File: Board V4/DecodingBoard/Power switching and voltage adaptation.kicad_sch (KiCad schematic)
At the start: 19 parts, among them U2 TPS7A7200RGW, U4 TPS2121RUXR

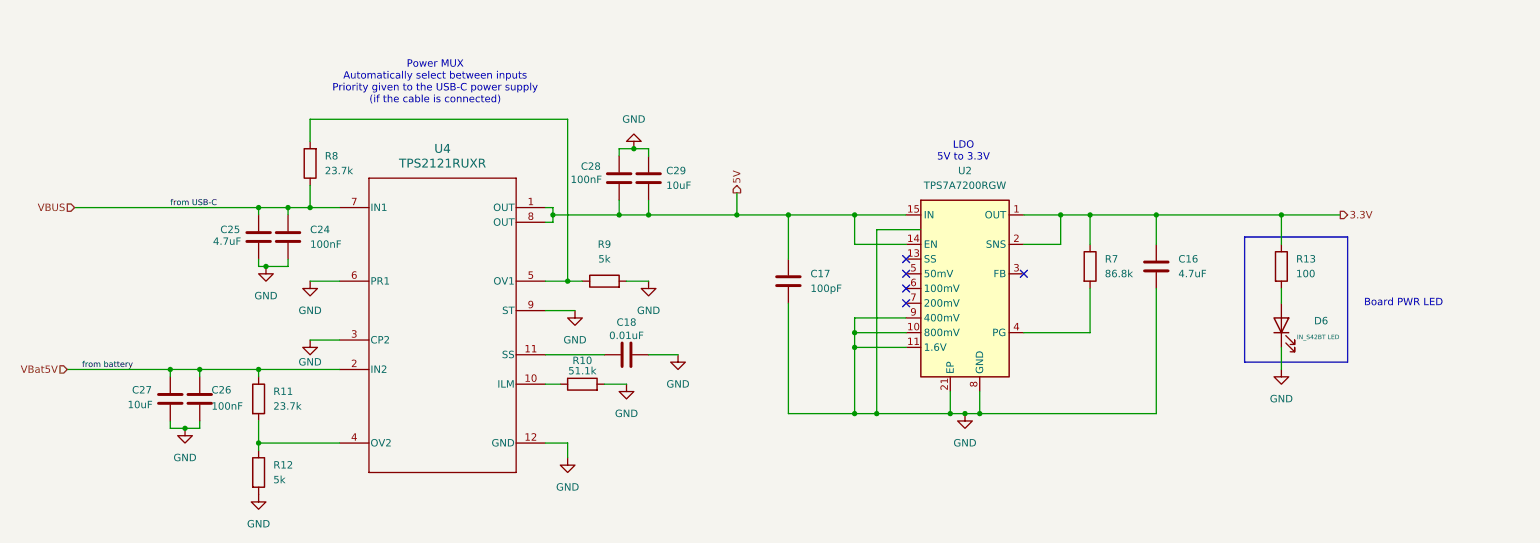
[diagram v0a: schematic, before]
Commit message: update to the LDO footprint and C16 from 4.7 uF to 10 uF
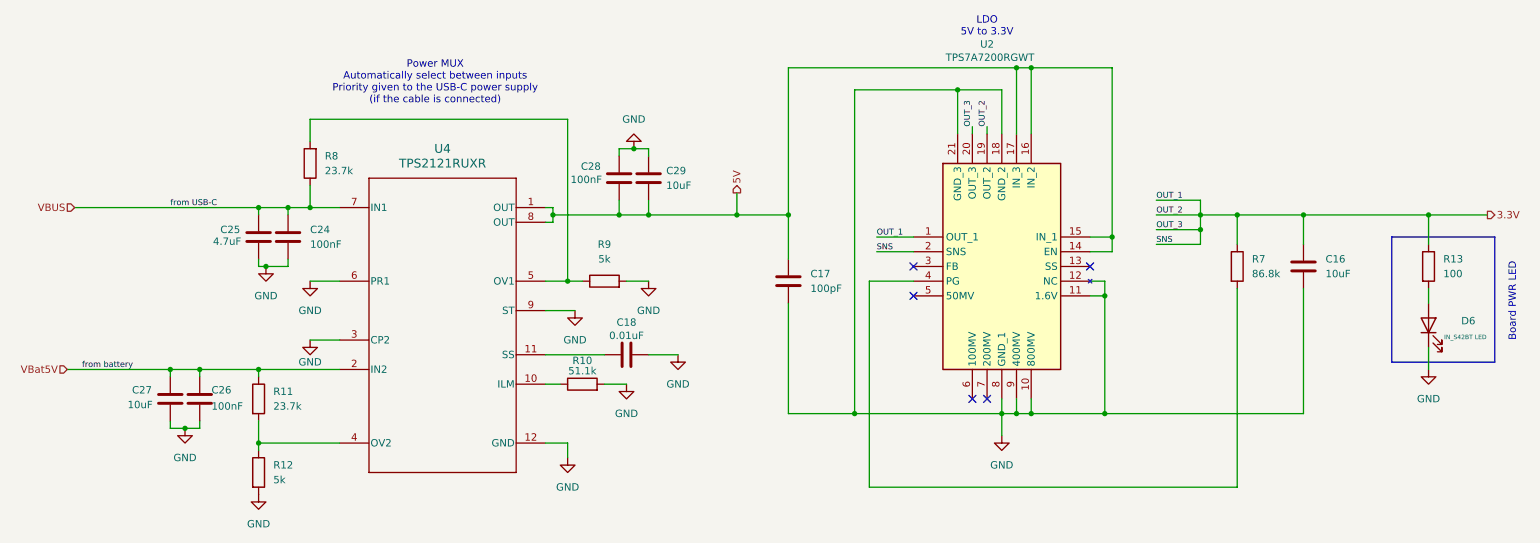
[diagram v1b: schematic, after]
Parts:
- removed U2: TPS7A7200RGW, Package_DFN_QFN:Texas_RGW0020A_VQFN-20-1EP_5x5mm_P0.65mm_EP3.15x3.15mm_ThermalVias, symbol Regulator_Linear:TPS7A7200RGW
- added U2: TPS7A7200RGWT, QFN65P500X500X100-21N-D, symbol TPS7A7200RGWT:TPS7A7200RGWT
- C16: value 4.7uF -> 10uF
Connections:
- net 3.3V: now also U2.1 (OUT_1), U2.19 (OUT_2), U2.2 (SNS), U2.20 (OUT_3)
- net 5V: now also U2.14 (EN), U2.15 (IN_1), U2.16 (IN_2), U2.17 (IN_3)
- net GND: now also U2.10 (800MV), U2.11 (1.6V), U2.12 (NC), U2.18 (GND_2), U2.21 (GND_3), U2.8 (GND_1), U2.9 (400MV)
- net at R7.2: now also U2.4 (PG)
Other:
- moved on the sheet: C16, D6, R13, R7

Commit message: Addition of the BLE module and BOM
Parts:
- C16, C17, C25, C27, C29: footprint (none) -> Capacitor_SMD:C_0603_1608Metric
- C18, C24, C26, C28: footprint (none) -> Capacitor_SMD:C_0402_1005Metric
- R10, R11, R12, R13, R8, R9: footprint (none) -> Resistor_SMD:R_0402_1005Metric
- R7: footprint (none) -> Resistor_SMD:R_0603_1608Metric
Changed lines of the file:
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@@
 	(title_block
 		(title "Power Switching and voltage adaptation")
-		(date "2026-09-29")
+		(date "2026-10-05")
 		(company "N-Pulse")
 		(comment 1 "Perrine Beurier")
@@
 	)
 	(junction
+		(at 34.29 59.69)
+		(diameter 0)
+		(color 0 0 0 0)
+	)
+	(junction
 		(at 111.76 60.96)
 		(diameter 0)
@@
 	)
 	(junction
+		(at 33.02 87.63)
+		(diameter 0)
+		(color 0 0 0 0)
+	)
+	(junction
 		(at 60.96 87.63)
 		(diameter 0)
@@
 	(wire
 		(pts
-			(xy 29.21 59.69) (xy 66.04 59.69)
+			(xy 29.21 59.69) (xy 34.29 59.69)
 		)
 		(stroke
@@
 	(wire
 		(pts
+			(xy 34.29 59.69) (xy 66.04 59.69)
+		)
+		(stroke
+			(width 0)
+			(type default)
+		)
+	)
+	(wire
+		(pts
 			(xy 60.96 100.33) (xy 60.96 101.6)
 		)
@@
 	)
 	(label "from battery"
-		(at 30.48 87.63 0)
+		(at 35.56 87.63 0)
 		(effects
 			(font
@@
 	)
 	(label "from USB-C"
-		(at 45.72 59.69 0)
+		(at 40.64 59.69 0)
 		(effects
 			(font
@@
 			)
 		)
-		(property "Footprint" ""
+		(property "Footprint" "Capacitor_SMD:C_0402_1005Metric"
 			(at 51.7652 96.52 0)
 			(hide yes)
@@
 			)
 		)
-		(property "Footprint" ""
+		(property "Footprint" "Capacitor_SMD:C_0603_1608Metric"
 			(at 129.2352 58.42 0)
 			(hide yes)
@@
 			)
 		)
-		(property "Footprint" ""
+		(property "Footprint" "Resistor_SMD:R_0402_1005Metric"
 			(at 261.112 69.85 90)
 			(hide yes)
@@
 			)
 		)
-		(property "Footprint" ""
+		(property "Footprint" "Resistor_SMD:R_0402_1005Metric"
 			(at 116.84 91.948 90)
 			(hide yes)
@@
 			)
 		)
-		(property "Footprint" ""
+		(property "Footprint" "Resistor_SMD:R_0603_1608Metric"
 			(at 228.092 69.85 90)
 			(hide yes)
@@
 			)
 		)
-		(property "Footprint" ""
+		(property "Footprint" "Capacitor_SMD:C_0603_1608Metric"
 			(at 242.2652 73.66 0)
 			(hide yes)
@@
 			)
 		)
-		(property "Footprint" ""
+		(property "Footprint" "Capacitor_SMD:C_0402_1005Metric"
 			(at 128.27 84.1248 0)
 			(hide yes)
@@
 			)
 		)
-		(property "Footprint" ""
+		(property "Footprint" "Capacitor_SMD:C_0402_1005Metric"
 			(at 124.1552 58.42 0)
 			(hide yes)
@@
 			)
 		)
-		(property "Footprint" ""
+		(property "Footprint" "Capacitor_SMD:C_0603_1608Metric"
 			(at 61.9252 68.58 0)
 			(hide yes)
@@
 			)
 		)
-		(property "Footprint" ""
+		(property "Footprint" "Resistor_SMD:R_0402_1005Metric"
 			(at 59.182 105.41 90)
 			(hide yes)
@@
 			)
 		)
-		(property "Footprint" ""
+		(property "Footprint" "Resistor_SMD:R_0402_1005Metric"
 			(at 59.182 92.71 90)
 			(hide yes)
@@
 	)
 	(symbol
+		(lib_id "power:PWR_FLAG")
+		(at 34.29 59.69 0)
+		(unit 1)
+		(body_style 1)
+		(exclude_from_sim no)
+		(in_bom yes)
+		(on_board yes)
+		(in_pos_files yes)
+		(dnp no)
+		(fields_autoplaced yes)
+		(property "Reference" "#FLG01"
+			(at 34.29 57.785 0)
+			(hide yes)
+			(show_name no)
+			(do_not_autoplace no)
+			(effects
+				(font
+					(size 1.27 1.27)
+				)
+			)
+		)
+		(property "Value" "PWR_FLAG"
+			(at 34.29 54.61 0)
+			(show_name no)
+			(do_not_autoplace no)
+			(effects
+				(font
+					(size 1.27 1.27)
+				)
+			)
+		)
+		(property "Footprint" "Package_SO:TSSOP-28_4.4x9.7mm_P0.65mm"
+			(at 34.29 59.69 0)
+			(hide yes)
+			(show_name no)
+			(do_not_autoplace no)
+			(effects
+				(font
+					(size 1.27 1.27)
+				)
+			)
+		)
+		(property "Datasheet" ""
+			(at 34.29 59.69 0)
+			(hide yes)
+			(show_name no)
+			(do_not_autoplace no)
+			(effects
+				(font
+					(size 1.27 1.27)
+				)
+			)
+		)
+		(property "Description" "Special symbol for telling ERC where power comes from"
+			(at 34.29 59.69 0)
+			(hide yes)
+			(show_name no)
+			(do_not_autoplace no)
+			(effects
+				(font
+					(size 1.27 1.27)
+				)
+			)
+		)
+		(pin "1"
+		)
+		(instances
+			(project "DecodingBoard"
+				(path "/b438bce8-ca67-4245-91ae-f4475acc63f6/f08b2c2d-ab65-459a-bbea-ee6098bc9100"
+					(reference "#FLG01")
+					(unit 1)
+				)
+			)
+		)
+	)
+	(symbol
 		(lib_id "Device:LED")
 		(at 262.89 80.01 90)
@@
 			)
 		)
-		(property "Footprint" ""
+		(property "Footprint" "Capacitor_SMD:C_0603_1608Metric"
 			(at 153.3652 76.2 0)
 			(hide yes)
@@
 			)
 		)
-		(property "Footprint" ""
+		(property "Footprint" "Resistor_SMD:R_0402_1005Metric"
 			(at 120.65 74.168 90)
 			(hide yes)
@@
 	)
 	(symbol
+		(lib_id "power:PWR_FLAG")
+		(at 33.02 87.63 0)
+		(unit 1)
+		(body_style 1)
+		(exclude_from_sim no)
+		(in_bom yes)
+		(on_board yes)
+		(in_pos_files yes)
+		(dnp no)
+		(fields_autoplaced yes)
+		(property "Reference" "#FLG02"
+			(at 33.02 85.725 0)
+			(hide yes)
+			(show_name no)
+			(do_not_autoplace no)
+			(effects
+				(font
+					(size 1.27 1.27)
+				)
+			)
+		)
+		(property "Value" "PWR_FLAG"
+			(at 33.02 82.55 0)
+			(show_name no)
+			(do_not_autoplace no)
+			(effects
+				(font
+					(size 1.27 1.27)
+				)
+			)
+		)
+		(property "Footprint" ""
+			(at 33.02 87.63 0)
+			(hide yes)
+			(show_name no)
+			(do_not_autoplace no)
+			(effects
+				(font
+					(size 1.27 1.27)
+				)
+			)
+		)
+		(property "Datasheet" ""
+			(at 33.02 87.63 0)
+			(hide yes)
+			(show_name no)
+			(do_not_autoplace no)
+			(effects
+				(font
+					(size 1.27 1.27)
+				)
+			)
+		)
+		(property "Description" "Special symbol for telling ERC where power comes from"
+			(at 33.02 87.63 0)
+			(hide yes)
+			(show_name no)
+			(do_not_autoplace no)
+			(effects
+				(font
+					(size 1.27 1.27)
+				)
+			)
+		)
+		(pin "1"
+		)
+		(instances
+			(project "DecodingBoard"
+				(path "/b438bce8-ca67-4245-91ae-f4475acc63f6/f08b2c2d-ab65-459a-bbea-ee6098bc9100"
+					(reference "#FLG02")
+					(unit 1)
+				)
+			)
+		)
+	)
+	(symbol
 		(lib_id "power:GND")
 		(at 69.85 72.39 0)
@@
 			)
 		)
-		(property "Footprint" ""
+		(property "Footprint" "Resistor_SMD:R_0402_1005Metric"
 			(at 71.628 52.07 90)
 			(hide yes)
@@
 			)
 		)
-		(property "Footprint" ""
+		(property "Footprint" "Capacitor_SMD:C_0402_1005Metric"
 			(at 67.0052 68.58 0)
 			(hide yes)
@@
 			)
 		)
-		(property "Footprint" ""
+		(property "Footprint" "Capacitor_SMD:C_0603_1608Metric"
 			(at 46.6852 96.52 0)
 			(hide yes)

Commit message: footprints updates
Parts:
- U2: footprint QFN65P500X500X100-21N-D -> Footprints:QFN65P500X500X100-21N-D
- U4: footprint RUX0012A -> Footprints:TPS2121RUXR
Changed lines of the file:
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@@
 			)
 		)
-		(property "Footprint" "RUX0012A"
+		(property "Footprint" "Footprints:TPS2121RUXR"
 			(at 92.71 80.01 0)
 			(hide yes)
@@
 			)
 		)
-		(property "Footprint" "QFN65P500X500X100-21N-D"
+		(property "Footprint" "Footprints:QFN65P500X500X100-21N-D"
 			(at 200.66 149.53 0)
 			(hide yes)

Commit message: First version of the layout
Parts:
- added C2: 220pF, Capacitor_SMD:C_0402_1005Metric, symbol Device:C
- C17: value 100pF -> 10uF
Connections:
- net 3.3V: now also C2.1
- net GND: no longer U4.6 (PR1)
- net VBUS: now also U4.6 (PR1)
- net FB: now reaches U2.3 (FB)
- net FB: now also C2.2
- no-connect marks 5 -> 4
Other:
- moved on the sheet: C16, R7
